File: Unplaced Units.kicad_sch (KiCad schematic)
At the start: 2 parts, among them U4 LM324, U5 LM339

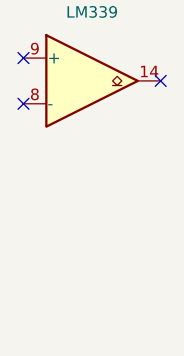
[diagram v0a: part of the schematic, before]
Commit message: Finished recreating the schematic
Created new footprints for DC Barrel Jack and Fuse Holder (3d models still require adjustment and finalize shunt resistance value and footprint)
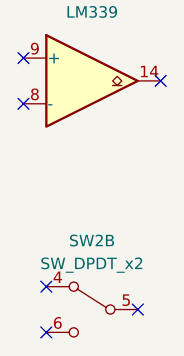
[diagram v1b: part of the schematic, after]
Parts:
- added SW2: SW_DPDT_x2, Button_Switch_THT:SW_Push_2P2T_Toggle_CK_PVA2xxH1xxxxxxV2, symbol Switch:SW_DPDT_x2
- U4: footprint (none) -> Package_SO:SO-14_3.9x8.65mm_P1.27mm; Local Seller (none) -> https://makerselectronics.com/product/lm324-sop-14-operatio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
- U5: footprint (none) -> Package_SO:SOIC-14_3.9x8.7mm_P1.27mm; Local Seller (none) -> https://makerselectronics.com/product/lm339d-5mv-0-25ua-4-s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
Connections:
- no-connect marks 12 -> 15
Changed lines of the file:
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@@
   (paper "A4")
   (no_connect (at 43.18 104.14))
+  (no_connect (at 55.88 148.59))
   (no_connect (at 43.18 125.73))
+  (no_connect (at 45.72 146.05))
   (no_connect (at 43.18 33.02))
   (no_connect (at 58.42 101.6))
+  (no_connect (at 45.72 151.13))
   (no_connect (at 58.42 35.56))
   (no_connect (at 43.18 38.1))
@@
       (effects (font (size 1.27 1.27)))
     )
-    (property "Footprint" "" (at 49.53 33.02 0)
+    (property "Footprint" "Package_SO:SO-14_3.9x8.65mm_P1.27mm" (at 49.53 33.02 0)
       (effects (font (size 1.27 1.27)) hide)
     )
     (property "Datasheet" "http://www.ti.com/lit/ds/symlink/lm2902-n.pdf" (at 52.07 30.48 0)
+      (effects (font (size 1.27 1.27)) hide)
+    )
+    (property "Local Seller" "https://makerselectronics.com/product/lm324-sop-14-operational-amplifier-smd" (at 50.8 35.56 0)
       (effects (font (size 1.27 1.27)) hide)
     )
@@
       (effects (font (size 1.27 1.27)))
     )
-    (property "Footprint" "" (at 49.53 99.06 0)
+    (property "Footprint" "Package_SO:SOIC-14_3.9x8.7mm_P1.27mm" (at 49.53 99.06 0)
       (effects (font (size 1.27 1.27)) hide)
     )
     (property "Datasheet" "https://www.st.com/resource/en/datasheet/lm139.pdf" (at 52.07 96.52 0)
+      (effects (font (size 1.27 1.27)) hide)
+    )
+    (property "Local Seller" "https://makerselectronics.com/product/lm339d-5mv-0-25ua-4-soic-14-comparator-smd-ic" (at 50.8 101.6 0)
       (effects (font (size 1.27 1.27)) hide)
     )
@@
       (effects (font (size 1.27 1.27)))
     )
-    (property "Footprint" "" (at 49.53 120.65 0)
+    (property "Footprint" "Package_SO:SOIC-14_3.9x8.7mm_P1.27mm" (at 49.53 120.65 0)
       (effects (font (size 1.27 1.27)) hide)
     )
     (property "Datasheet" "https://www.st.com/resource/en/datasheet/lm139.pdf" (at 52.07 118.11 0)
+      (effects (font (size 1.27 1.27)) hide)
+    )
+    (property "Local Seller" "https://makerselectronics.com/product/lm339d-5mv-0-25ua-4-soic-14-comparator-smd-ic" (at 50.8 123.19 0)
       (effects (font (size 1.27 1.27)) hide)
     )
@@
     )
   )
+  (symbol (lib_id "Switch:SW_DPDT_x2") (at 50.8 148.59 0) (mirror y) (unit 2)
+    (in_bom yes) (on_board yes) (dnp no) (fields_autoplaced)
+    (property "Reference" "SW2" (at 50.8 140.97 0)
+      (effects (font (size 1.27 1.27)))
+    )
+    (property "Value" "SW_DPDT_x2" (at 50.8 143.51 0)
+      (effects (font (size 1.27 1.27)))
+    )
+    (property "Footprint" "Button_Switch_THT:SW_Push_2P2T_Toggle_CK_PVA2xxH1xxxxxxV2" (at 50.8 148.59 0)
+      (effects (font (size 1.27 1.27)) hide)
+    )
+    (property "Datasheet" "~" (at 50.8 148.59 0)
+      (effects (font (size 1.27 1.27)) hide)
+    )
+    (property "Local Seller" "https://makerselectronics.com/product/push-button-6-pins-self-lock-8x8mm" (at 50.8 148.59 0)
+      (effects (font (size 1.27 1.27)) hide)
+    )
+    (pin "1")
+    (pin "2")
+    (pin "3")
+    (pin "4")
+    (pin "5")
+    (pin "6")
+    (instances
+      (project "[EXOTIC] AVR Kit"
+        (path "/bd689b4b-40d7-46ba-91b6-965ce30f8212/9da448d2-dd3c-46c7-b716-b331cd5a4621"
+          (reference "SW2") (unit 2)
+        )
+        (path "/bd689b4b-40d7-46ba-91b6-965ce30f8212/9da448d2-dd3c-46c7-b716-b331cd5a4621/bbc5b563-1e1e-48b3-9d6e-3409d51ecb1f"
+          (reference "SW2") (unit 2)
+        )
+      )
+    )
+  )
   (symbol (lib_id "Comparator:LM339") (at 50.8 71.12 0) (unit 2)
     (in_bom yes) (on_board yes) (dnp no) (fields_autoplaced)
@@
       (effects (font (size 1.27 1.27)))
     )
-    (property "Footprint" "" (at 49.53 68.58 0)
+    (property "Footprint" "Package_SO:SOIC-14_3.9x8.7mm_P1.27mm" (at 49.53 68.58 0)
       (effects (font (size 1.27 1.27)) hide)
     )
@@
       (effects (font (size 1.27 1.27)) hide)
     )
+    (property "Local Seller" "https://makerselectronics.com/product/lm339d-5mv-0-25ua-4-soic-14-comparator-smd-ic" (at 50.8 71.12 0)
+      (effects (font (size 1.27 1.27)) hide)
+    )

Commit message: WIP2
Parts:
- removed SW2: SW_DPDT_x2, Button_Switch_THT:SW_Push_2P2T_Toggle_CK_PVA2xxH1xxxxxxV2, symbol Switch:SW_DPDT_x2
- removed U4: LM324, Package_SO:SO-14_3.9x8.65mm_P1.27mm, symbol Amplifier_Operational:LM324
- removed unit 4 of U5
- added SW2: SW_DPDT_x2, Button_Switch_THT:SW_Push_2P2T_Toggle_CK_PVA2xxH1xxxxxxV2, symbol Switch:SW_DPDT_x2
- added U4: LM324, Package_SO:SO-14_3.9x8.65mm_P1.27mm, symbol Amplifier_Operational:LM324
- added U5: LM339, Package_SO:SOIC-14_3.9x8.7mm_P1.27mm, symbol Comparator:LM339
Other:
- company: (none) -> Team Exotic
- title: (none) -> ATMEGA32A AVR Kit
- moved on the sheet: U5A, U5B

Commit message: done something
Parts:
- SW2: footprint Button_Switch_THT:SW_Push_2P2T_Toggle_CK_PVA2xxH1xxxxxxV2 -> M's Library:SW_Push_DPDT_Toggle_7.0mm
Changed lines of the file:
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@@
       (effects (font (size 1.27 1.27)))
     )
-    (property "Footprint" "Button_Switch_THT:SW_Push_2P2T_Toggle_CK_PVA2xxH1xxxxxxV2" (at 38.1 152.4 0)
+    (property "Footprint" "M's Library:SW_Push_DPDT_Toggle_7.0mm" (at 38.1 152.4 0)
       (effects (font (size 1.27 1.27)) hide)
     )

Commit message: Rev 3.1
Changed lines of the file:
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@@
   (no_connect (at 30.48 73.66))
   (no_connect (at 30.48 99.06))
-  (symbol (lib_id "Comparator:LM339") (at 38.1 101.6 0) (unit 2)
+  (symbol (lib_id "Comparator:LM339") (at 38.1 101.6 0) (unit 3)
     (in_bom yes) (on_board yes) (dnp no) (fields_autoplaced)
     (property "Reference" "U5" (at 38.1 91.44 0)
@@
       (project "[EXOTIC] AVR Kit"
         (path "/bd689b4b-40d7-46ba-91b6-965ce30f8212/9da448d2-dd3c-46c7-b716-b331cd5a4621/bbc5b563-1e1e-48b3-9d6e-3409d51ecb1f"
-          (reference "U5") (unit 2)
+          (reference "U5") (unit 3)
         )
       )
@@
         )
         (path "/bd689b4b-40d7-46ba-91b6-965ce30f8212/9da448d2-dd3c-46c7-b716-b331cd5a4621/bbc5b563-1e1e-48b3-9d6e-3409d51ecb1f"
-          (reference "U5") (unit 3)
+          (reference "U5") (unit 4)
         )
       )
@@
     )
   )
-  (symbol (lib_id "Comparator:LM339") (at 38.1 76.2 0) (unit 1)
+  (symbol (lib_id "Comparator:LM339") (at 38.1 76.2 0) (unit 2)
     (in_bom yes) (on_board yes) (dnp no) (fields_autoplaced)
     (property "Reference" "U5" (at 38.1 66.04 0)
@@
       (project "[EXOTIC] AVR Kit"
         (path "/bd689b4b-40d7-46ba-91b6-965ce30f8212/9da448d2-dd3c-46c7-b716-b331cd5a4621/bbc5b563-1e1e-48b3-9d6e-3409d51ecb1f"
-          (reference "U5") (unit 1)
+          (reference "U5") (unit 2)
         )
       )

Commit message: Pre Rev. 4
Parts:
- removed U4: LM324, Package_SO:SO-14_3.9x8.65mm_P1.27mm, symbol Amplifier_Operational:LM324
- removed U5: LM339, Package_SO:SOIC-14_3.9x8.7mm_P1.27mm, symbol Comparator:LM339
- added U4 (x3): LM324, Package_SO:SO-14_3.9x8.65mm_P1.27mm, symbol Amplifier_Operational:LM324
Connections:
- no-connect marks 15 -> 12
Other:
- moved on the sheet: SW2A
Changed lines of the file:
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@@
     (comment 1 "Author: Morad Tamer")
   )
-  (no_connect (at 30.48 104.14))
-  (no_connect (at 43.18 152.4))
-  (no_connect (at 30.48 130.81))
-  (no_connect (at 33.02 149.86))
+  (no_connect (at 30.48 59.69))
+  (no_connect (at 77.47 57.15))
+  (no_connect (at 67.31 54.61))
+  (no_connect (at 45.72 74.93))
   (no_connect (at 30.48 35.56))
-  (no_connect (at 45.72 101.6))
-  (no_connect (at 33.02 154.94))
+  (no_connect (at 67.31 59.69))
   (no_connect (at 45.72 38.1))
   (no_connect (at 30.48 40.64))
-  (no_connect (at 30.48 78.74))
-  (no_connect (at 45.72 76.2))
-  (no_connect (at 30.48 125.73))
-  (no_connect (at 45.72 128.27))
-  (no_connect (at 30.48 73.66))
-  (no_connect (at 30.48 99.06))
-  (symbol (lib_id "Comparator:LM339") (at 38.1 101.6 0) (unit 3)
+  (no_connect (at 30.48 72.39))
+  (no_connect (at 30.48 54.61))
+  (no_connect (at 30.48 77.47))
+  (no_connect (at 45.72 57.15))
+  (symbol (lib_id "Switch:SW_DPDT_x2") (at 72.39 57.15 0) (mirror y) (unit 1)
     (in_bom yes) (on_board yes) (dnp no) (fields_autoplaced)
-    (property "Reference" "U5" (at 38.1 91.44 0)
+    (property "Reference" "SW2" (at 72.39 49.53 0)
       (effects (font (size 1.27 1.27)))
     )
-    (property "Value" "LM339" (at 38.1 93.98 0)
+    (property "Value" "SW_DPDT_x2" (at 72.39 52.07 0)
       (effects (font (size 1.27 1.27)))
     )
-    (property "Footprint" "Package_SO:SOIC-14_3.9x8.7mm_P1.27mm" (at 36.83 99.06 0)
+    (property "Footprint" "M's Library:SW_Push_DPDT_Toggle_7.0mm" (at 72.39 57.15 0)
       (effects (font (size 1.27 1.27)) hide)
     )
-    (property "Datasheet" "https://www.st.com/resource/en/datasheet/lm139.pdf" (at 39.37 96.52 0)
+    (property "Datasheet" "~" (at 72.39 57.15 0)
       (effects (font (size 1.27 1.27)) hide)
     )
-    (property "Local Seller" "https://makerselectronics.com/product/lm339d-5mv-0-25ua-4-soic-14-comparator-smd-ic" (at 38.1 101.6 0)
-      (effects (font (size 1.27 1.27)) hide)
-    )
-    (pin "2")
-    (pin "4")
-    (pin "5")
-    (pin "1")
-    (pin "6")
-    (pin "7")
-    (pin "10")
-    (pin "11")
-    (pin "13")
-    (pin "14")
-    (pin "8")
-    (pin "9")
-    (pin "12")
-    (pin "3")
-    (instances
-      (project "[EXOTIC] AVR Kit"
-        (path "/bd689b4b-40d7-46ba-91b6-965ce30f8212/9da448d2-dd3c-46c7-b716-b331cd5a4621/bbc5b563-1e1e-48b3-9d6e-3409d51ecb1f"
-          (reference "U5") (unit 3)
-        )
-      )
-    )
-  )
-  (symbol (lib_id "Switch:SW_DPDT_x2") (at 38.1 152.4 0) (mirror y) (unit 1)
-    (in_bom yes) (on_board yes) (dnp no) (fields_autoplaced)
-    (property "Reference" "SW2" (at 38.1 144.78 0)
-      (effects (font (size 1.27 1.27)))
-    )
-    (property "Value" "SW_DPDT_x2" (at 38.1 147.32 0)
-      (effects (font (size 1.27 1.27)))
-    )
-    (property "Footprint" "M's Library:SW_Push_DPDT_Toggle_7.0mm" (at 38.1 152.4 0)
-      (effects (font (size 1.27 1.27)) hide)
-    )
-    (property "Datasheet" "~" (at 38.1 152.4 0)
-      (effects (font (size 1.27 1.27)) hide)
-    )
-    (property "Local Seller" "https://makerselectronics.com/product/push-button-6-pins-self-lock-8x8mm" (at 38.1 152.4 0)
+    (property "Local Seller" "https://makerselectronics.com/product/push-button-6-pins-self-lock-8x8mm" (at 72.39 57.15 0)
       (effects (font (size 1.27 1.27)) hide)
     )
@@
         )
         (path "/bd689b4b-40d7-46ba-91b6-965ce30f8212/9da448d2-dd3c-46c7-b716-b331cd5a4621/bbc5b563-1e1e-48b3-9d6e-3409d51ecb1f"
-          (reference "SW2") (unit 1)
-        )
-      )
-    )
-  )
-  (symbol (lib_id "Comparator:LM339") (at 38.1 128.27 0) (unit 1)
-    (in_bom yes) (on_board yes) (dnp no) (fields_autoplaced)
-    (property "Reference" "U5" (at 38.1 118.11 0)
-      (effects (font (size 1.27 1.27)))
-    )
-    (property "Value" "LM339" (at 38.1 120.65 0)
-      (effects (font (size 1.27 1.27)))
-    )
-    (property "Footprint" "Package_SO:SOIC-14_3.9x8.7mm_P1.27mm" (at 36.83 125.73 0)
-      (effects (font (size 1.27 1.27)) hide)
-    )
-    (property "Datasheet" "https://www.st.com/resource/en/datasheet/lm139.pdf" (at 39.37 123.19 0)
-      (effects (font (size 1.27 1.27)) hide)
-    )
-    (property "Local Seller" "https://makerselectronics.com/product/lm339d-5mv-0-25ua-4-soic-14-comparator-smd-ic" (at 38.1 128.27 0)
-      (effects (font (size 1.27 1.27)) hide)
-    )
-    (pin "2")
-    (pin "4")
-    (pin "5")
-    (pin "1")
-    (pin "6")
-    (pin "7")
-    (pin "10")
-    (pin "11")
-    (pin "13")
-    (pin "14")
-    (pin "8")
-    (pin "9")
-    (pin "12")
-    (pin "3")
-    (instances
-      (project "[EXOTIC] AVR Kit"
-        (path "/bd689b4b-40d7-46ba-91b6-965ce30f8212/9da448d2-dd3c-46c7-b716-b331cd5a4621"
-          (reference "U5") (unit 1)
-        )
-        (path "/bd689b4b-40d7-46ba-91b6-965ce30f8212/9da448d2-dd3c-46c7-b716-b331cd5a4621/bbc5b563-1e1e-48b3-9d6e-3409d51ecb1f"
-          (reference "U5") (unit 4)
+          (reference "SW2") (unit 2)
         )
       )
@@
         )
         (path "/bd689b4b-40d7-46ba-91b6-965ce30f8212/9da448d2-dd3c-46c7-b716-b331cd5a4621/bbc5b563-1e1e-48b3-9d6e-3409d51ecb1f"
-          (reference "U4") (unit 3)
+          (reference "U4") (unit 1)
         )
       )
     )
   )
-  (symbol (lib_id "Comparator:LM339") (at 38.1 76.2 0) (unit 2)
+  (symbol (lib_id "Amplifier_Operational:LM324") (at 38.1 57.15 0) (unit 3)
     (in_bom yes) (on_board yes) (dnp no) (fields_autoplaced)
-    (property "Reference" "U5" (at 38.1 66.04 0)
+    (property "Reference" "U4" (at 38.1 46.99 0)
       (effects (font (size 1.27 1.27)))
     )
-    (property "Value" "LM339" (at 38.1 68.58 0)
+    (property "Value" "LM324" (at 38.1 49.53 0)
       (effects (font (size 1.27 1.27)))
     )
-    (property "Footprint" "Package_SO:SOIC-14_3.9x8.7mm_P1.27mm" (at 36.83 73.66 0)
+    (property "Footprint" "Package_SO:SO-14_3.9x8.65mm_P1.27mm" (at 36.83 54.61 0)
       (effects (font (size 1.27 1.27)) hide)
     )
-    (property "Datasheet" "https://www.st.com/resource/en/datasheet/lm139.pdf" (at 39.37 71.12 0)
+    (property "Datasheet" "http://www.ti.com/lit/ds/symlink/lm2902-n.pdf" (at 39.37 52.07 0)
       (effects (font (size 1.27 1.27)) hide)
     )
-    (property "Local Seller" "https://makerselectronics.com/product/lm339d-5mv-0-25ua-4-soic-14-comparator-smd-ic" (at 38.1 76.2 0)
+    (property "Local Seller" "https://makerselectronics.com/product/lm324-sop-14-operational-amplifier-smd" (at 38.1 57.15 0)
       (effects (font (size 1.27 1.27)) hide)
     )
+    (pin "1")
     (pin "2")
-    (pin "4")
+    (pin "3")
     (pin "5")
-    (pin "1")
     (pin "6")
     (pin "7")
     (pin "10")
-    (pin "11")
-    (pin "13")
-    (pin "14")
     (pin "8")
     (pin "9")
     (pin "12")
-    (pin "3")
+    (pin "13")
+    (pin "14")
+    (pin "11")
+    (pin "4")
     (instances
       (project "[EXOTIC] AVR Kit"
+        (path "/bd689b4b-40d7-46ba-91b6-965ce30f8212/9da448d2-dd3c-46c7-b716-b331cd5a4621"
+          (reference "U4") (unit 3)
+        )
         (path "/bd689b4b-40d7-46ba-91b6-965ce30f8212/9da448d2-dd3c-46c7-b716-b331cd5a4621/bbc5b563-1e1e-48b3-9d6e-3409d51ecb1f"
-          (reference "U5") (unit 2)
+          (reference "U4") (unit 2)
         )
       )
+    )
+  )
+  (symbol (lib_id "Amplifier_Operational:LM324") (at 38.1 74.93 0) (unit 3)
+    (in_bom yes) (on_board yes) (dnp no) (fields_autoplaced)
+    (property "Reference" "U4" (at 38.1 64.77 0)
+      (effects (font (size 1.27 1.27)))
+    )
+    (property "Value" "LM324" (at 38.1 67.31 0)
+      (effects (font (size 1.27 1.27)))
+    )
+    (property "Footprint" "Package_SO:SO-14_3.9x8.65mm_P1.27mm" (at 36.83 72.39 0)
+      (effects (font (size 1.27 1.27)) hide)
+    )
+    (property "Datasheet" "http://www.ti.com/lit/ds/symlink/lm2902-n.pdf" (at 39.37 69.85 0)
+      (effects (font (size 1.27 1.27)) hide)
+    )
+    (property "Local Seller" "https://makerselectronics.com/product/lm324-sop-14-operational-amplifier-smd" (at 38.1 74.93 0)
+      (effects (font (size 1.27 1.27)) hide)
+    )
+    (pin "1")
+    (pin "2")
+    (pin "3")
+    (pin "5")
+    (pin "6")
+    (pin "7")
+    (pin "10")
+    (pin "8")
+    (pin "9")
+    (pin "12")
+    (pin "13")
+    (pin "14")
+    (pin "11")
+    (pin "4")
+    (instances
+      (project "[EXOTIC] AVR Kit"
+        (path "/bd689b4b-40d7-46ba-91b6-965ce30f8212/9da448d2-dd3c-46c7-b716-b331cd5a4621"
+          (reference "U4") (unit 3)
+        )
+        (path "/bd689b4b-40d7-46ba-91b6-965ce30f8212/9da448d2-dd3c-46c7-b716-b331cd5a4621/bbc5b563-1e1e-48b3-9d6e-3409d51ecb1f"
+          (reference "U4") (unit 4)
+        )
+      )

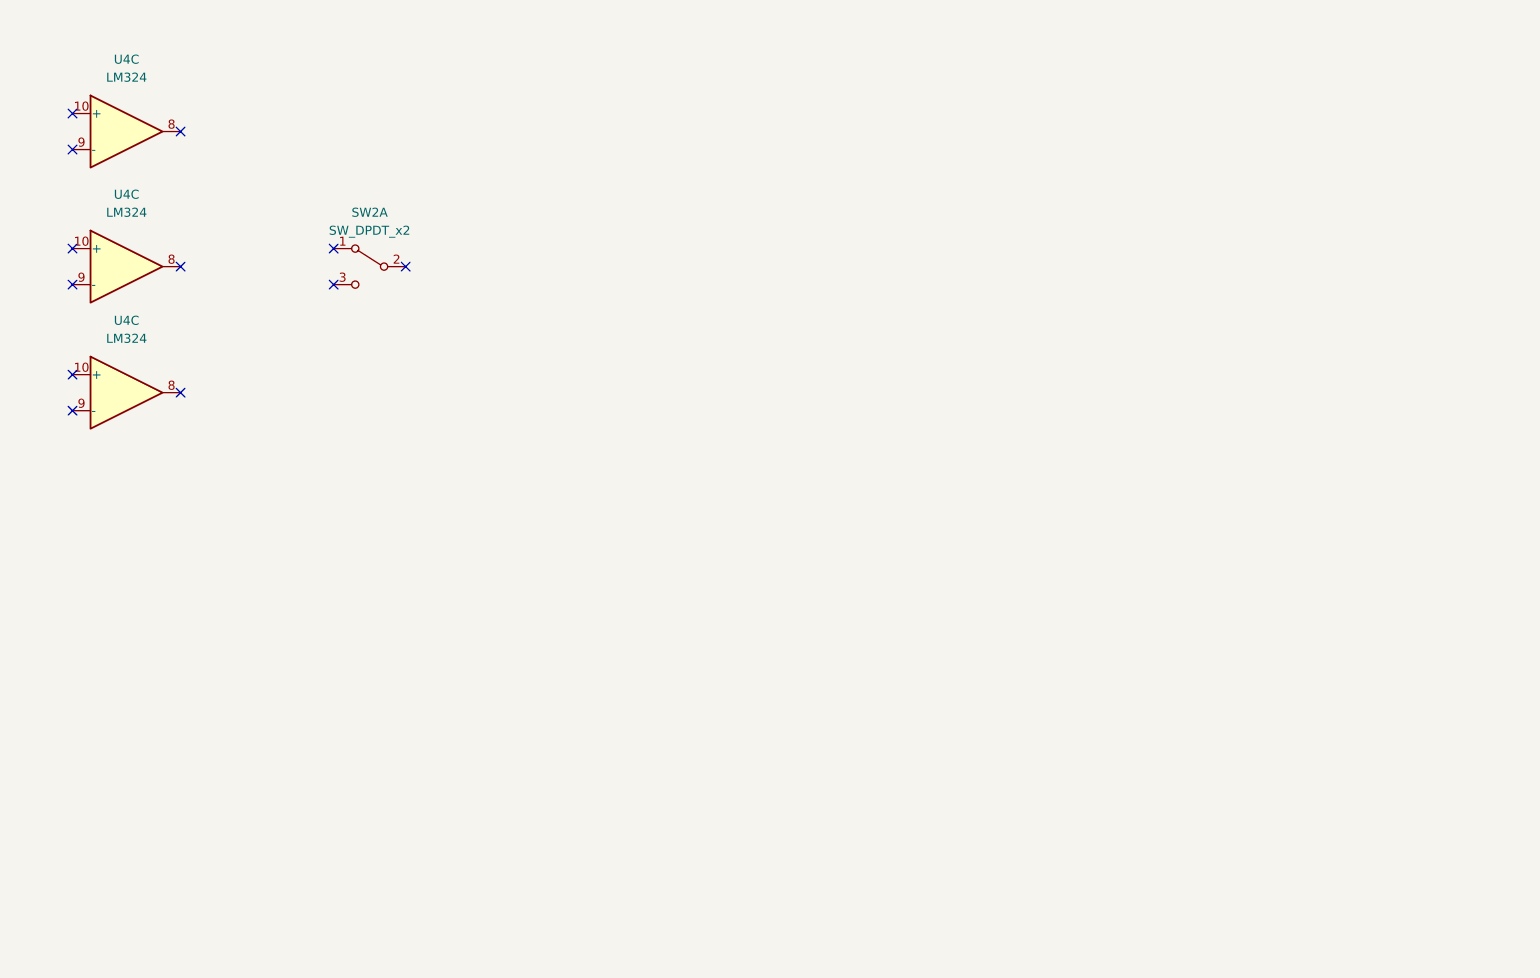
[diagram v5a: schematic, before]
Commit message: Migrated from KiCAD 7.0 to 8.0
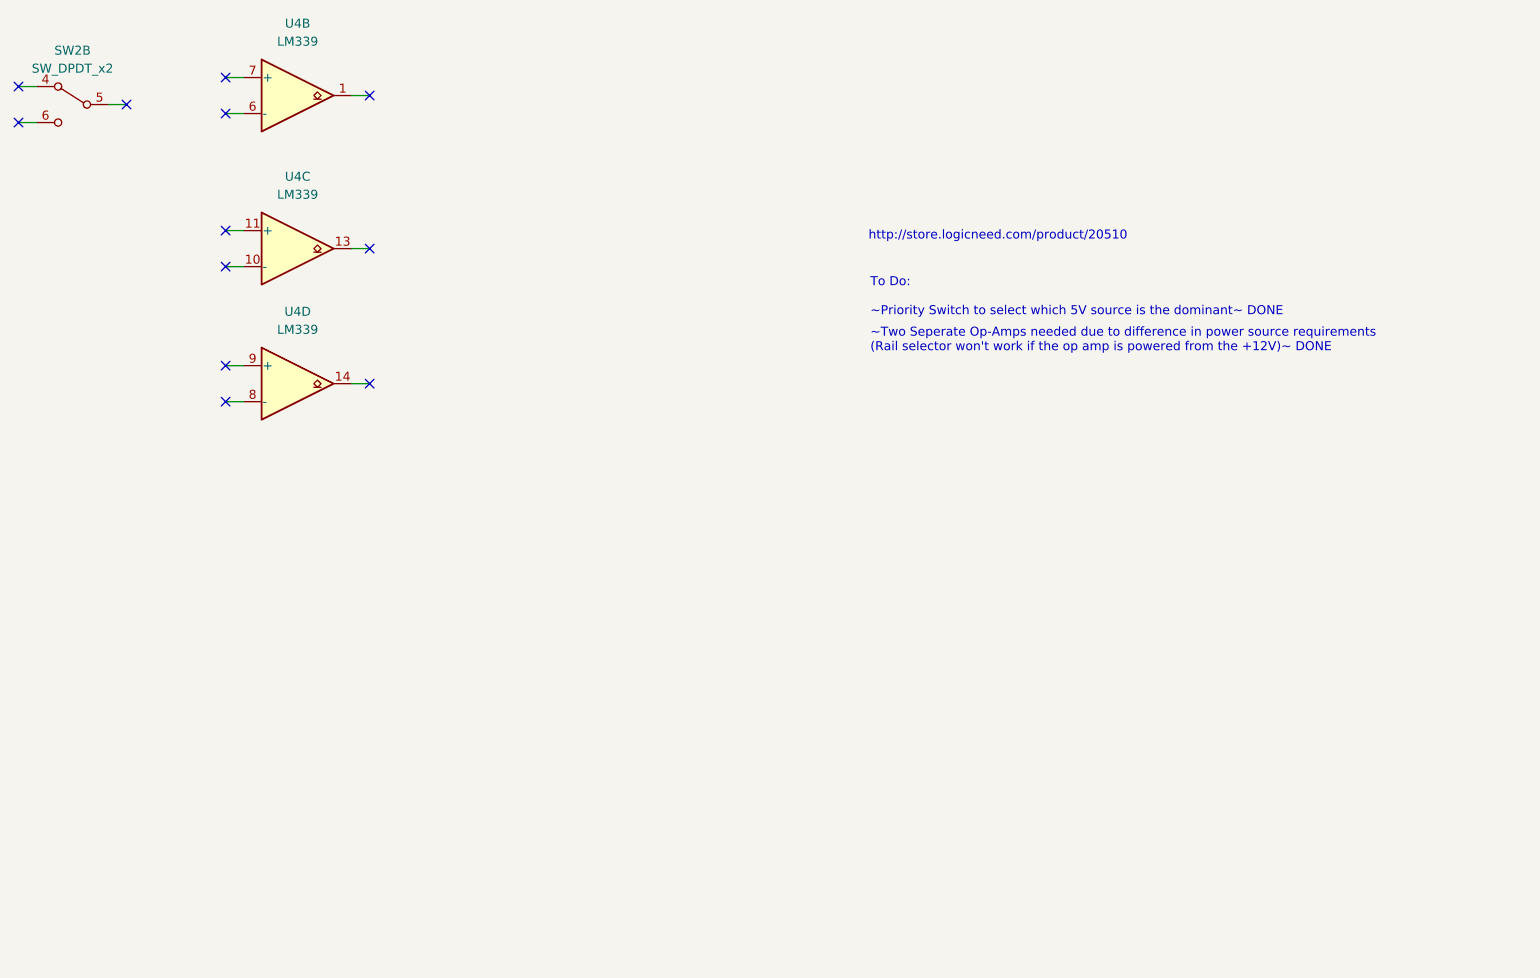
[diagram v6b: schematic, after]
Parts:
- removed U4 (x3): LM324, Package_SO:SO-14_3.9x8.65mm_P1.27mm, symbol Amplifier_Operational:LM324
- added U4: LM339, Package_SO:SOIC-14_3.9x8.7mm_P1.27mm, symbol Comparator:LM339
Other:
- note added: "To Do: ~Priority Switch to select which 5V source is the dominant~ DONE"
- note added: "http://store.logicneed.com/product/20510"
- note added: "~Two Seperate Op-Amps needed due to difference in power source requirements (Rail selector won't work if the op amp is powered from the +12V)~ DONE"
- moved on the sheet: SW2B
